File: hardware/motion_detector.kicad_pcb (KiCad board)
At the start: 2 copper layers, 45 x 25 mm, 16 parts, among them P1 CON-SENSOR, U1 M24C64, U2 HC-SR501, U3 DRILL, U4 DRILL, U5 DRILL, U6 DRILL

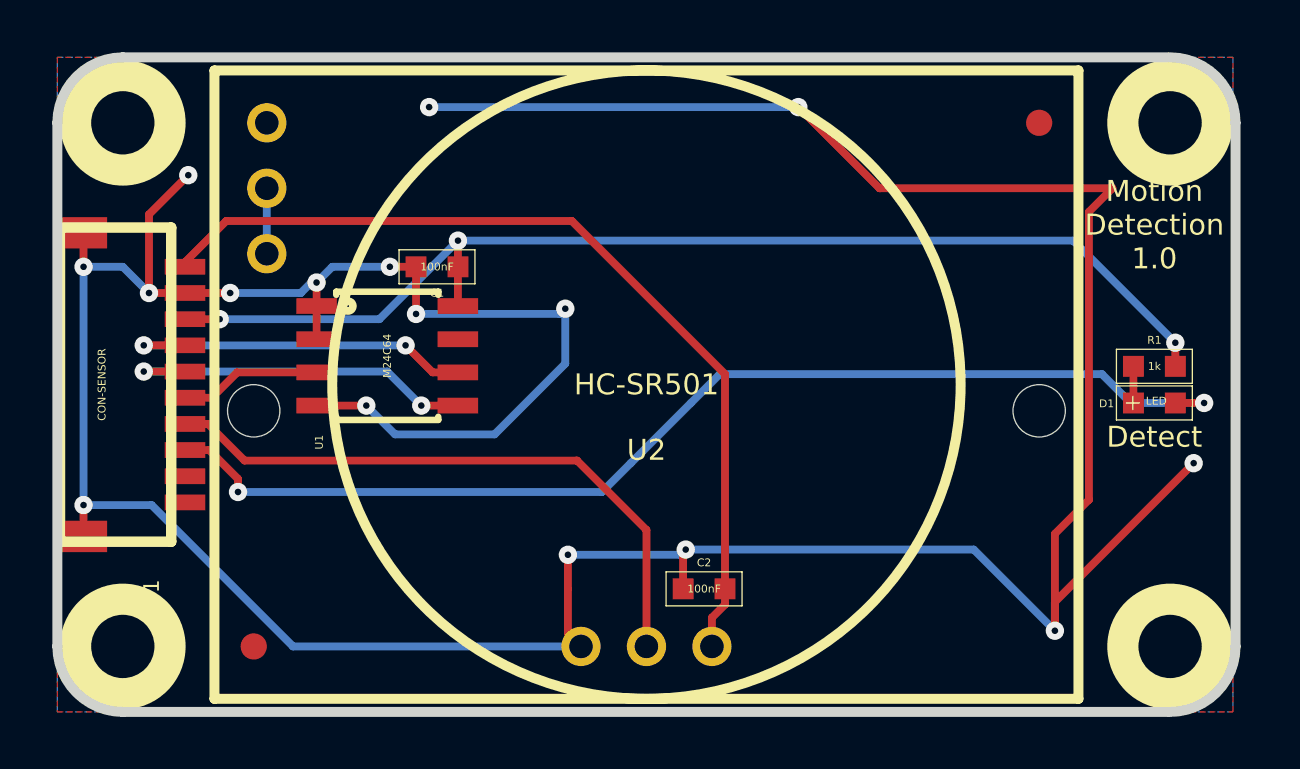
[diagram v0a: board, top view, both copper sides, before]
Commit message: remove big silkscreen lines
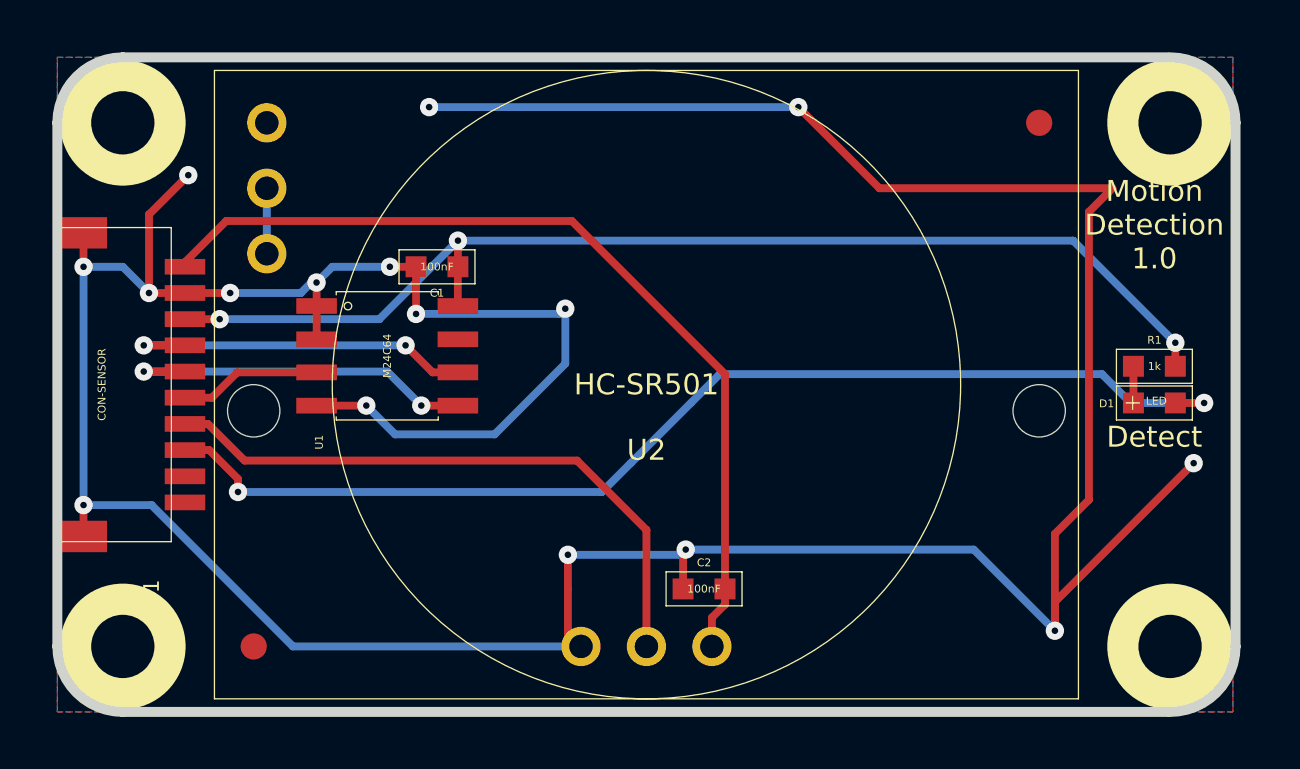
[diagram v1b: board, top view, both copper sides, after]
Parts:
- P1: footprint CON-SENSOR -> tinkerforge:CON-SENSOR
- U1: footprint SOIC8 -> tinkerforge:SOIC8
- U2: footprint HC-SR501 -> tinkerforge:HC-SR501
